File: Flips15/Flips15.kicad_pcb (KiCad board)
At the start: 2 copper layers, 100 x 100 mm, 59 parts, among them CN1 UFP2810, U1001 74HC238, U1002 ULN2803A, U1003 74HC238, U1004 TBD62783A, U1101 74HC238, U1102 ULN2803A, U1103 74HC238, U1104 TBD62783A, U701 74HC238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

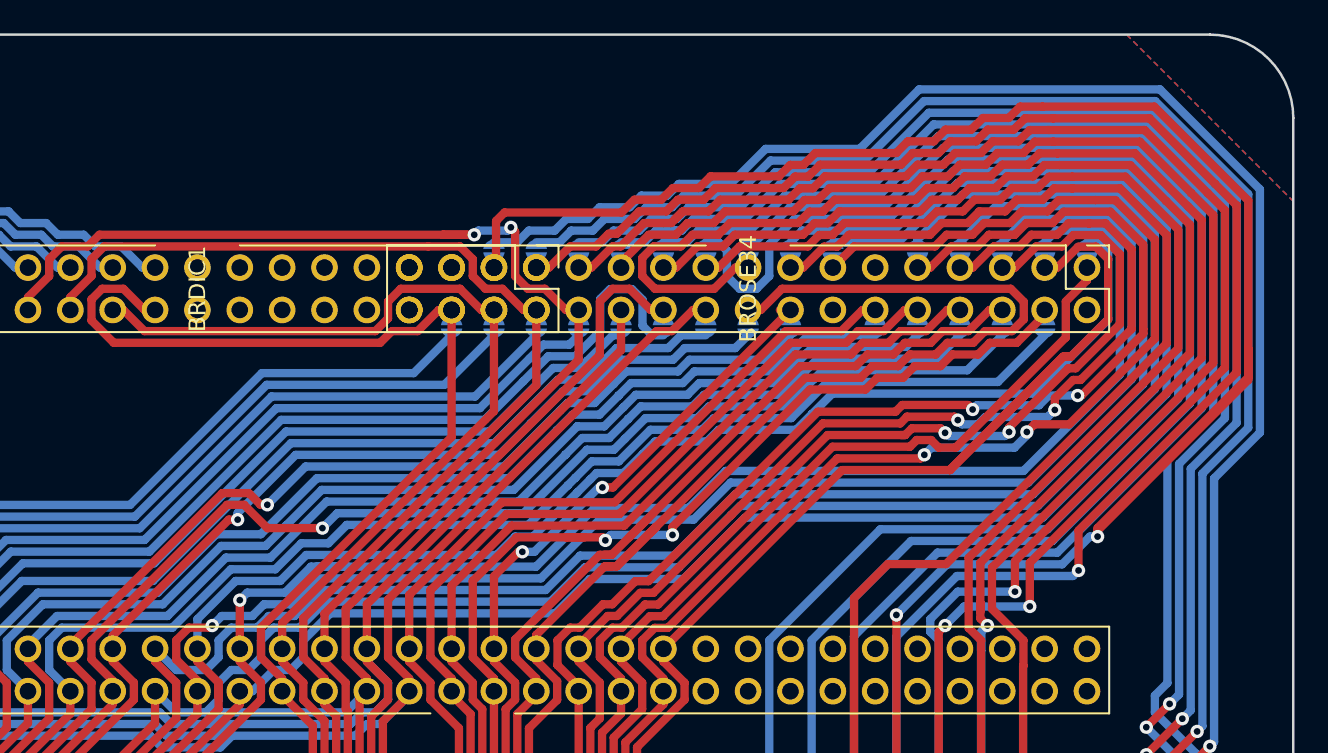
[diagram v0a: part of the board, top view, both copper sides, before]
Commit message: more traces for Flips15
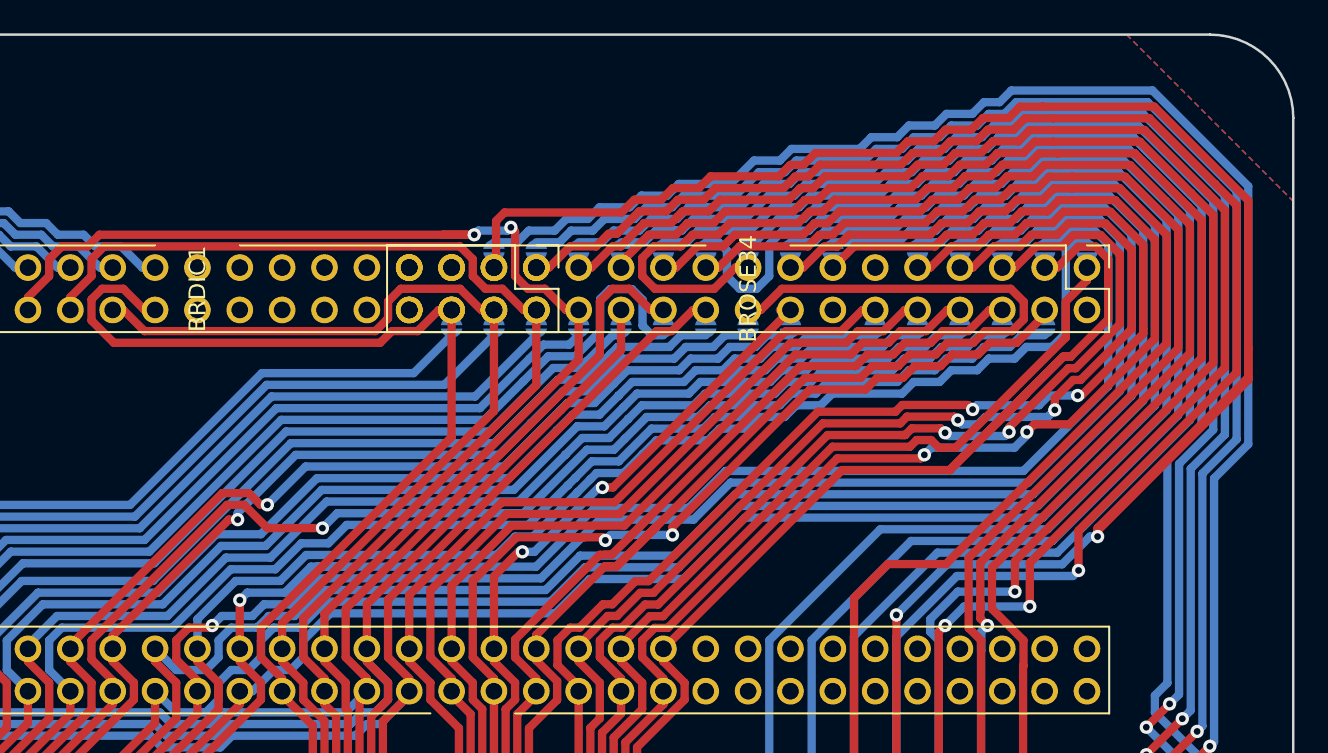
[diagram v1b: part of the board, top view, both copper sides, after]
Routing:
- net /SY27: track 142.5 -> 147.9 mm
- net /SY18: track 105.7 -> 103.6 mm
- net /SY15: track 119.9 -> 118.8 mm
- net /SY24: track 139.5 -> 138.5 mm
- net /SY22: track 134.2 -> 133.3 mm
- net /SY26: track 118.7 -> 117.7 mm
- net /SY25: track 138.5 -> 137.6 mm
- net /SY28: track 116.9 -> 116.0 mm
- net /SY19: track 131.8 -> 130.9 mm
- net /SY16: track 118.1 -> 117.2 mm
- net /SY23: track 132.8 -> 131.9 mm
- net /SY20: track 118.9 -> 118.0 mm
- net /SY17: track 113.6 -> 112.8 mm
- net /SY21: track 143.4 -> 142.5 mm

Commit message: tracing Flips15
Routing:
- net /SY27: track 147.9 -> 129.1 mm, vias 0 -> 1
- net /X22: track 140.8 -> 126.3 mm
- net /SY25: track 137.6 -> 125.3 mm, vias 2 -> 1
- net /X20: track 97.7 -> 87.7 mm
- net /X28: track 126.2 -> 129.0 mm
- net /SY23: track 131.9 -> 129.6 mm
- net /X24: track 118.5 -> 119.9 mm
- net /X19: track 106.7 -> 108.1 mm
- net /X21: track 106.7 -> 105.3 mm
- net /X25: track 115.6 -> 116.9 mm
- net /SY24: track 138.5 -> 137.5 mm, vias 2 -> 0
- net /SY19: track 130.9 -> 130.0 mm
- net /SY21: track 142.5 -> 141.6 mm
- net /SY20: track 118.0 -> 117.1 mm
- net /SY17: track 112.8 -> 111.9 mm
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
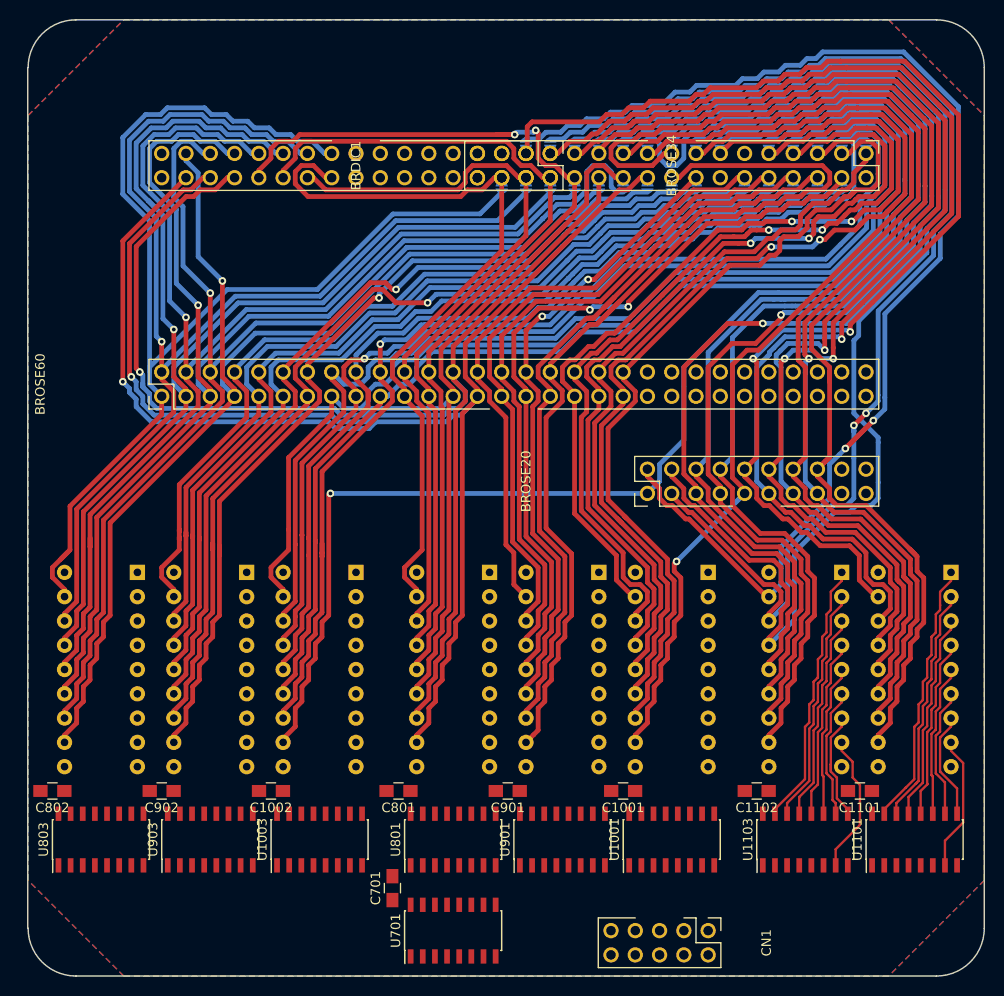
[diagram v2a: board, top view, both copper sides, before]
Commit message: Adding more solder jumpers to overlapping pins of BRDIC1 and BROSE34
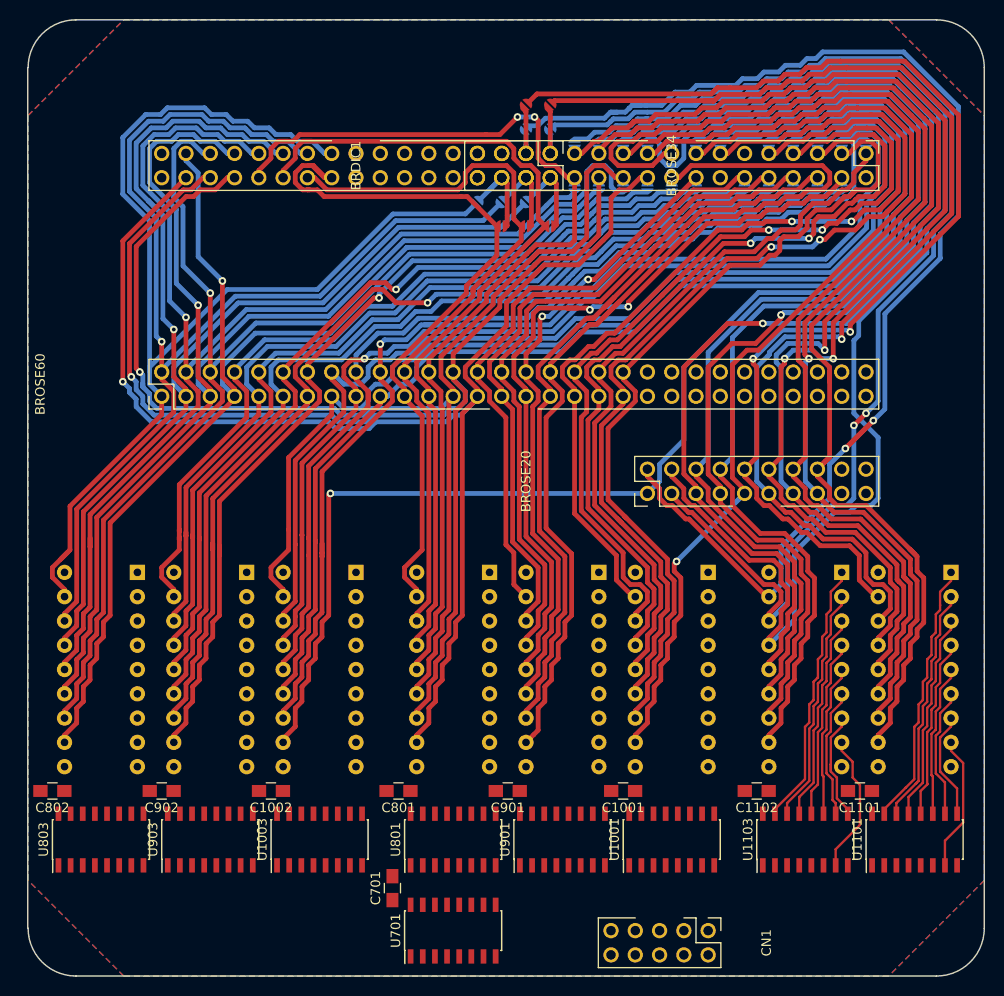
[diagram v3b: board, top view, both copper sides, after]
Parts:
- added JP129: Jumper_NO_Small, Own:SolderJumper1.3mmNoSilk, F.Cu at (105.4, 59.7)
- added JP130: Jumper_NO_Small, Own:SolderJumper1.3mmNoSilk, F.Cu at (105.4, 72.4)
- added JP131: Jumper_NO_Small, Own:SolderJumper1.3mmNoSilk, F.Cu at (102.9, 59.7)
- added JP132: Jumper_NO_Small, Own:SolderJumper1.3mmNoSilk, F.Cu at (102.9, 72.4)
- added JP133: Jumper_NO_Small, Own:SolderJumper1.3mmNoSilk, F.Cu at (100.3, 72.4)
- moved JP102 2.96 mm to (100.3, 69.8), turned to 45 degrees
- moved JP101 2.96 mm to (97.8, 69.8), turned to 45 degrees
- moved JP103 2.96 mm to (102.9, 69.8), turned to 45 degrees
- moved JP122 1.52 mm to (102.9, 62.2), turned to 225 degrees
- moved JP123 1.52 mm to (105.4, 62.2), turned to 225 degrees
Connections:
- BRDIC1 pad 27: /X23 -> /T1
- BRDIC1 pad 28: /X3 -> /T2
- BRDIC1 pad 29: /X22 -> /T3
- BRDIC1 pad 30: /X2 -> /T4
- BRDIC1 pad 32: /X1 -> /T6
- BROSE20 pad 10: /X22 -> /~RY22
- BROSE20 pad 11: /X23 -> /~RY23
- BROSE34 pad 1: /X23 -> /T1
- BROSE34 pad 2: /X3 -> /T2
- BROSE34 pad 20: /X1 -> /~RY1
- BROSE34 pad 22: /X2 -> /~RY2
- BROSE34 pad 24: /X3 -> /~RY3
- BROSE34 pad 3: /X22 -> /T3
- BROSE34 pad 4: /X2 -> /T4
- BROSE34 pad 6: /X1 -> /T6
- BROSE60 pad 21: /X1 -> /~RY1
- BROSE60 pad 22: /X2 -> /~RY2
- BROSE60 pad 23: /X3 -> /~RY3
- JP101 pad 2: /X1 -> /T6
- JP102 pad 2: /X2 -> /T4
- JP103 pad 2: /X3 -> /T2
- JP122 pad 2: /X22 -> /T3
- JP123 pad 2: /X23 -> /T1
- U1102 pad 16: /X23 -> /~RY23
- U1102 pad 17: /X22 -> /~RY22
- U802 pad 15: /X3 -> /~RY3
- U802 pad 16: /X2 -> /~RY2
- U802 pad 17: /X1 -> /~RY1
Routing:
- net /X22: track 126.3 -> 0.00 mm, vias 2 -> 0
- net /~RY22: track 0.00 -> 122.4 mm, vias 0 -> 2
- net /X23: track 122.3 -> 0.00 mm, vias 1 -> 0
- net /~RY23: track 0.00 -> 121.6 mm, vias 0 -> 1
- net /X3: track 89.0 -> 0.00 mm
- net /~RY3: track 0.00 -> 88.5 mm
- net /X1: track 80.0 -> 0.00 mm
- net /X2: track 78.8 -> 0.00 mm
- net /~RY2: track 0.00 -> 78.2 mm
- net /~RY1: track 0.00 -> 77.7 mm
- net /T2: track 0.00 -> 10.3 mm
- net /T6: track 0.00 -> 10.2 mm
- net /T4: track 0.00 -> 8.43 mm
- net /T3: track 0.00 -> 7.80 mm
- net /T1: track 0.00 -> 7.80 mm
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
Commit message: more tracing Flips15
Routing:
- net /X7: track 138.6 -> 137.0 mm
- net /X6: track 135.2 -> 133.8 mm
- net /X5: track 133.3 -> 131.9 mm
- net /X4: track 103.2 -> 101.8 mm
- net /~RY23: track 121.6 -> 120.4 mm
- net GND: vias 0 -> 23

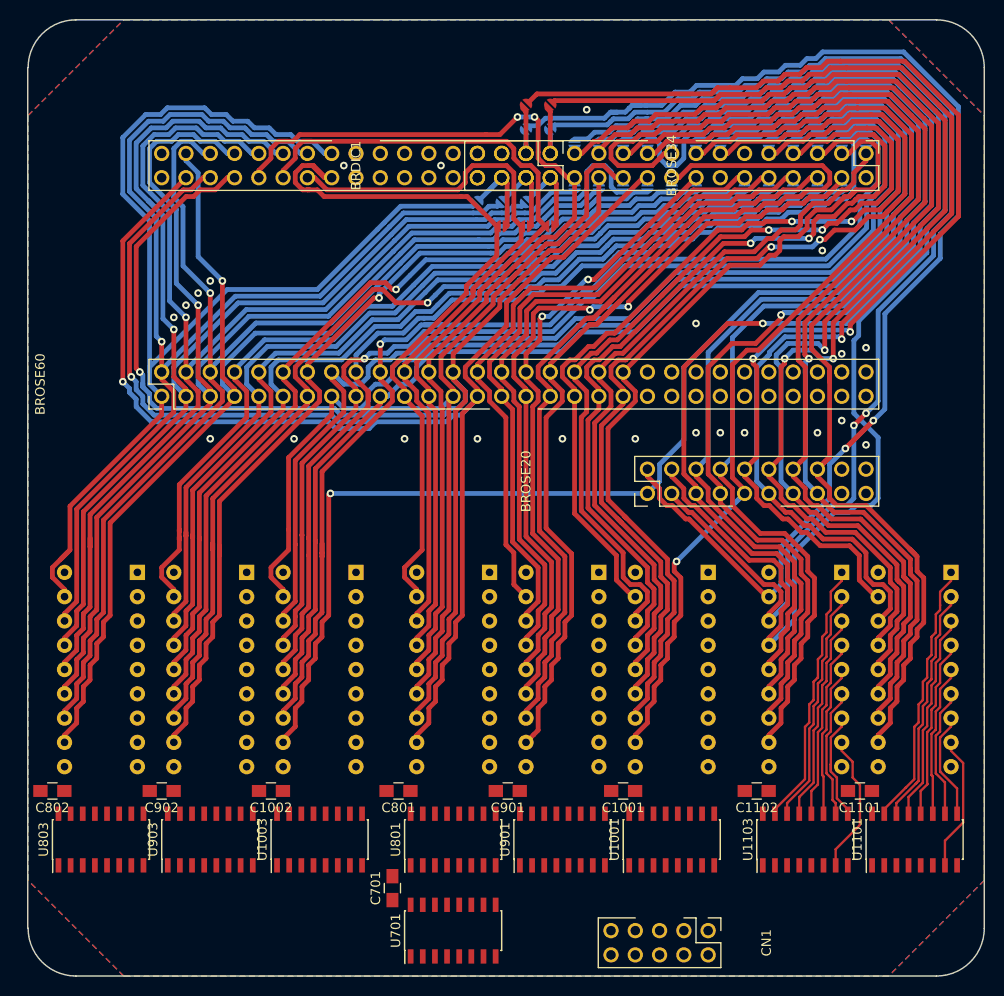
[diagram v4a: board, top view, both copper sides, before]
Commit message: adding mounting holes, more traces
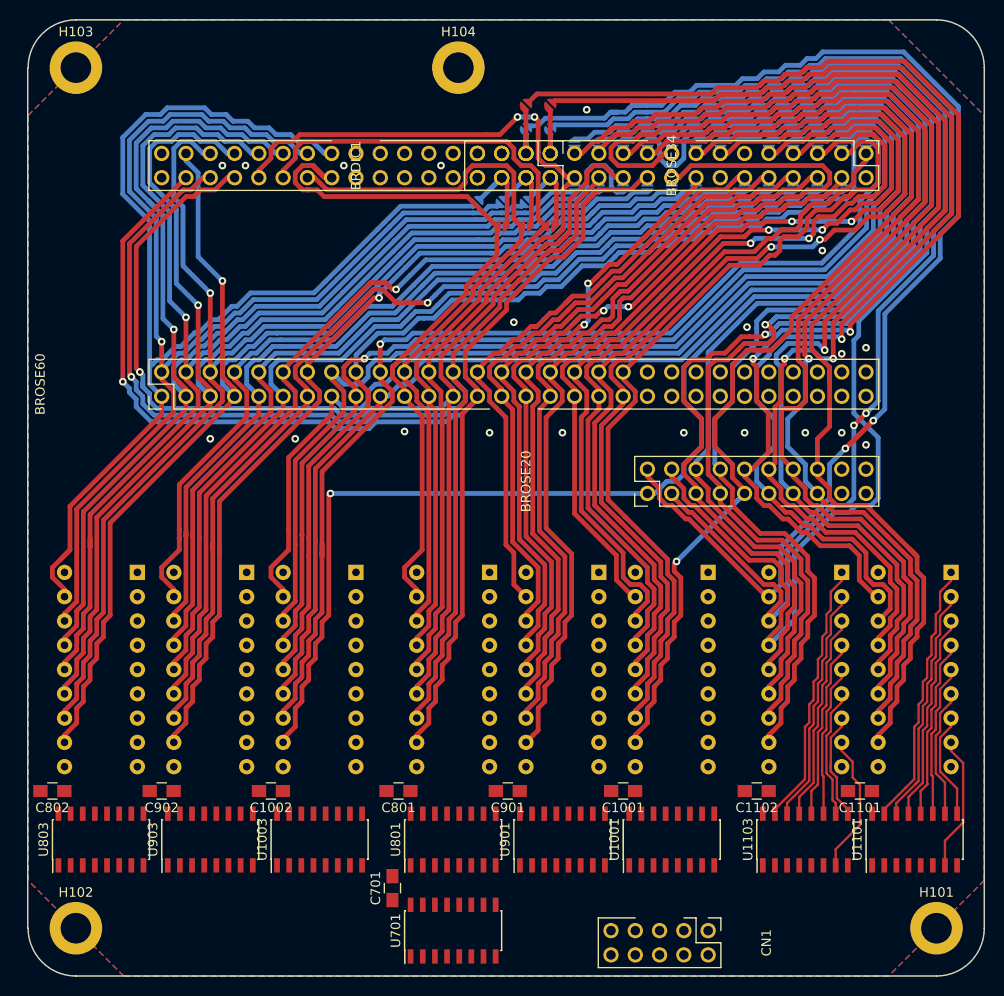
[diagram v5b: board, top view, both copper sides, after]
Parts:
- added H101: MountingHole, Mounting_Holes:MountingHole_3.2mm_M3_ISO14580_Pad, F.Cu at (145.8, 145.8)
- added H102: MountingHole, Mounting_Holes:MountingHole_3.2mm_M3_ISO14580_Pad, F.Cu at (55.8, 145.8)
- added H103: MountingHole, Mounting_Holes:MountingHole_3.2mm_M3_ISO14580_Pad, F.Cu at (55.8, 55.8)
- added H104: MountingHole, Mounting_Holes:MountingHole_3.2mm_M3_ISO14580_Pad, F.Cu at (95.8, 55.8)
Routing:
- net /X14: track 104.3 -> 100.8 mm
- net /SY27: track 129.1 -> 132.2 mm
- net /SY21: track 141.6 -> 144.2 mm
- net /X11: track 80.7 -> 78.4 mm
- net /X21: track 105.3 -> 107.6 mm
- net /X10: track 72.4 -> 70.3 mm
- net /X26: track 105.7 -> 107.6 mm
- net /SY20: track 117.1 -> 115.2 mm
- net /X28: track 129.0 -> 127.2 mm
- net /X7: track 137.0 -> 138.5 mm
- net /SY25: track 125.3 -> 126.8 mm
- net /X27: track 112.8 -> 114.3 mm
- net /~RY23: track 120.4 -> 121.9 mm
- net /X12: track 65.5 -> 67.0 mm
- net /~RY22: track 122.4 -> 123.9 mm
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
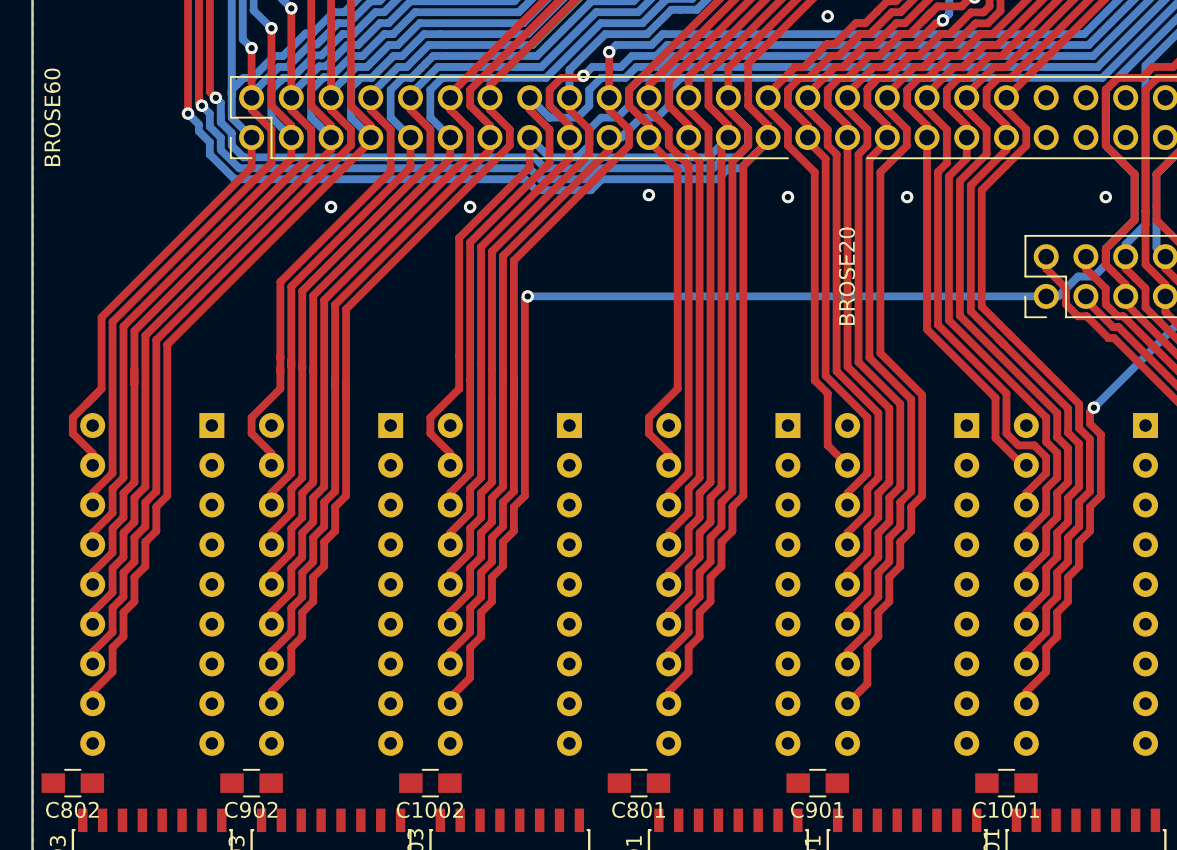
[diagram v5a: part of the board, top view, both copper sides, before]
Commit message: move driver ics to get more space for decoders and control connector
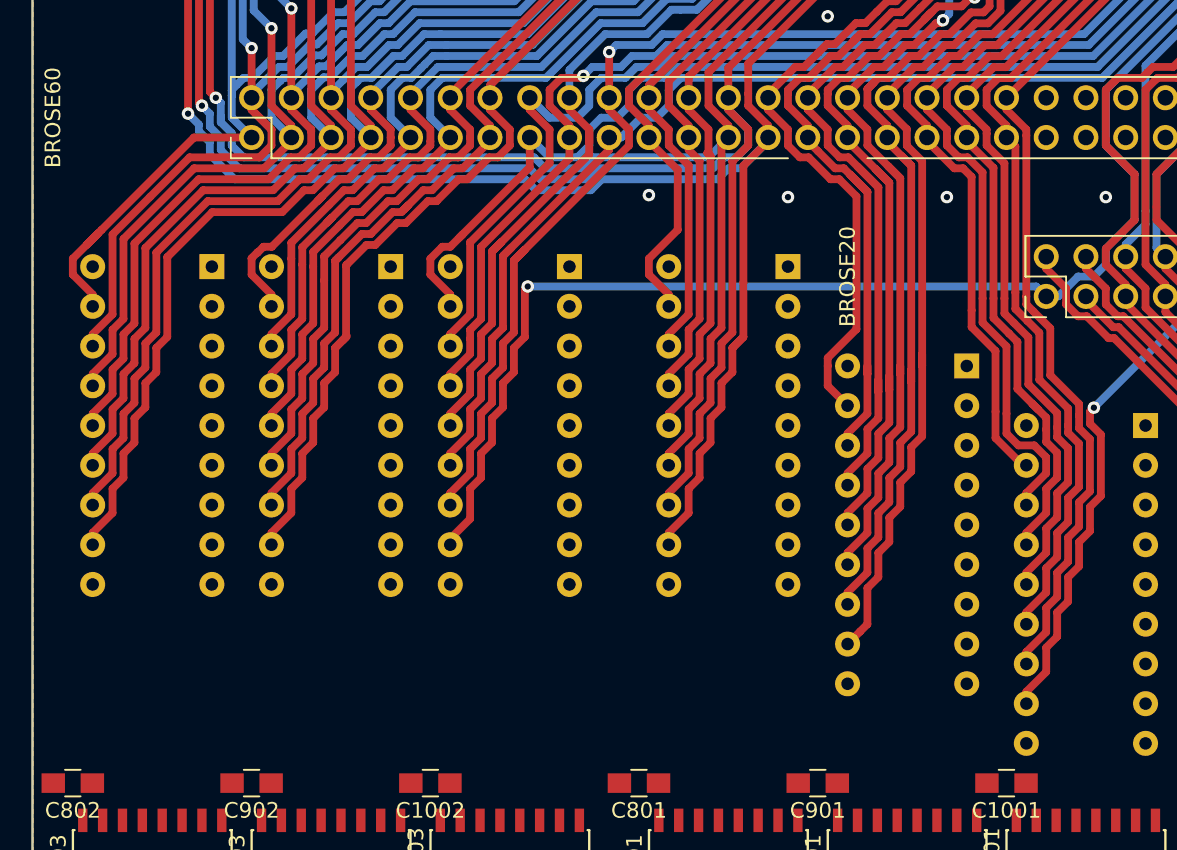
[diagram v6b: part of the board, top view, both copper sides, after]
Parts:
- moved U1004 10.2 mm to (85.1, 98.4)
- moved U802 10.2 mm to (99.1, 98.4)
- moved U804 10.2 mm to (62.2, 98.4)
- moved U904 10.2 mm to (73.7, 98.4)
- moved U902 3.81 mm to (110.5, 104.8)
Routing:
- net /SY20: track 115.2 -> 104.6 mm
- net /SY16: track 116.3 -> 106.1 mm
- net /X6: track 133.8 -> 123.6 mm
- net /~RY2: track 78.2 -> 68.0 mm
- net /~RY3: track 88.5 -> 78.3 mm
- net /~RY1: track 77.7 -> 67.5 mm
- net /SY17: track 112.5 -> 102.3 mm
- net /SY9: track 93.4 -> 83.5 mm
- net /X4: track 101.8 -> 92.0 mm
- net /SY19: track 130.0 -> 120.4 mm
- net /SY15: track 117.9 -> 108.4 mm
- net /X5: track 132.1 -> 122.5 mm
- net /SY18: track 103.6 -> 94.3 mm
- net /SY11: track 104.3 -> 95.0 mm
- net /SY21: track 144.2 -> 134.9 mm
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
